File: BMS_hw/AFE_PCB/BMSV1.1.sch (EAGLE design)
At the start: 293 parts, among them IC1 MC33771BEP, IC10 TLP152-COUPLERTOSHIBA, IC11 TLP152-COUPLERTOSHIBA, IC2 SFH6156-1, IC3 MIC28515V1, IC7 SFH6156-1, IC8 SFH6156-1, IC9 TLP152-COUPLERTOSHIBA, Q1 IRLML5203, Q2 SI2392ADS-T1-GE3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

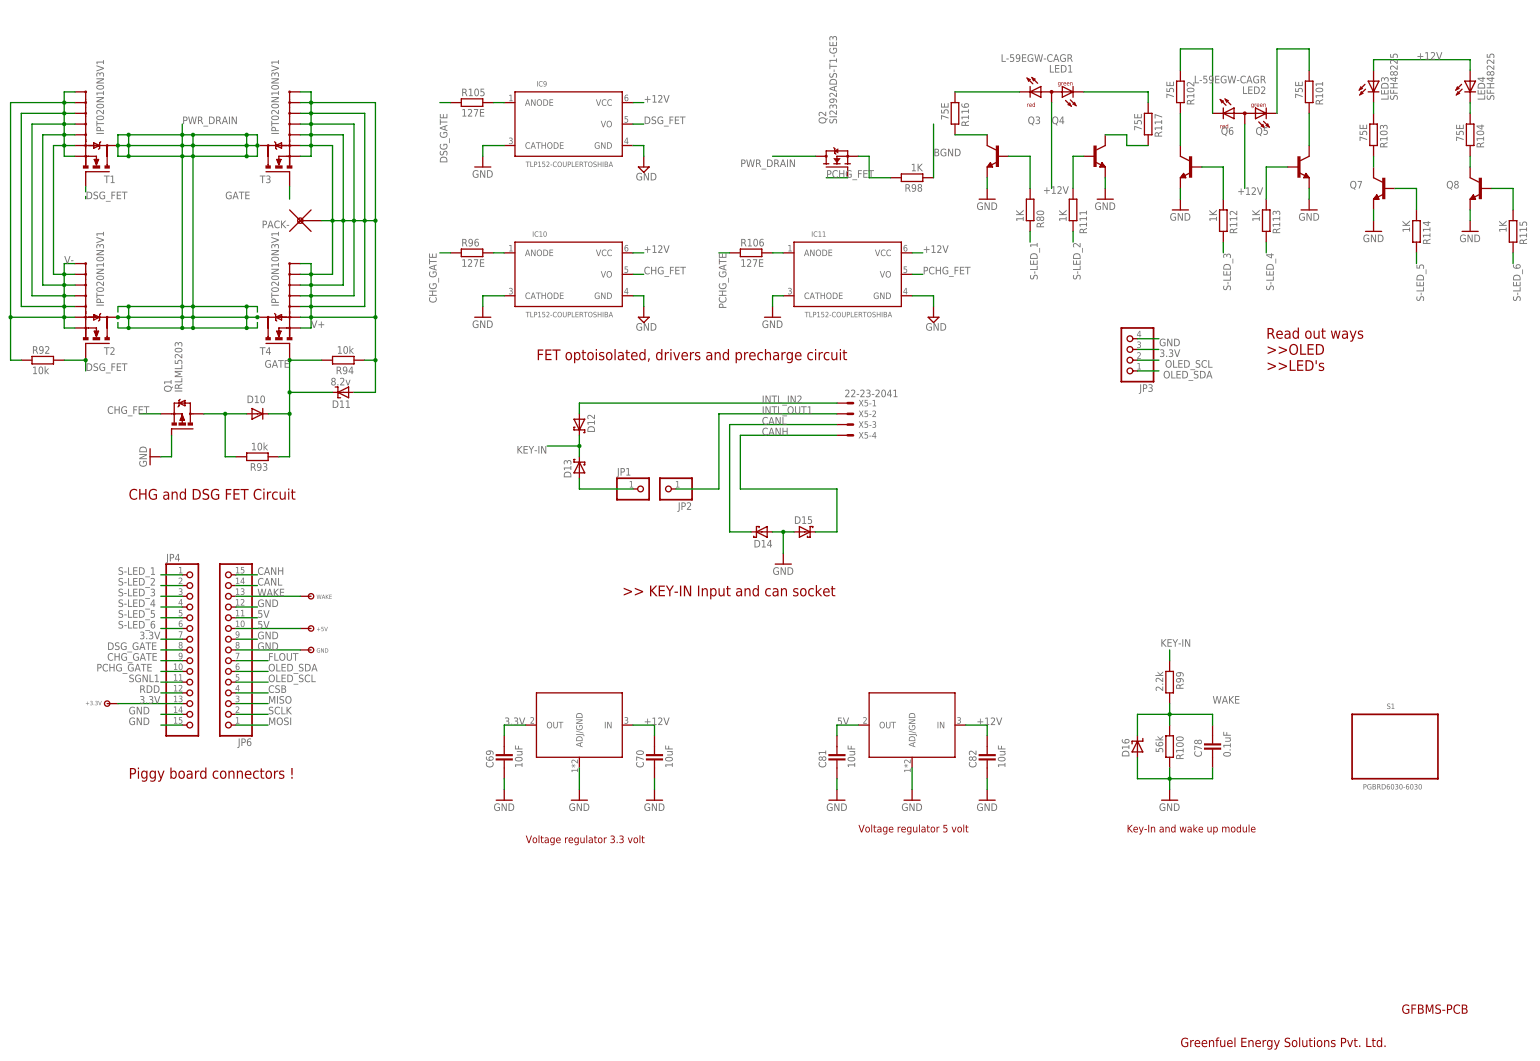
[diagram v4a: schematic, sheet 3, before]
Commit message: updated afe shmetatic rectification stage of MCU PCB
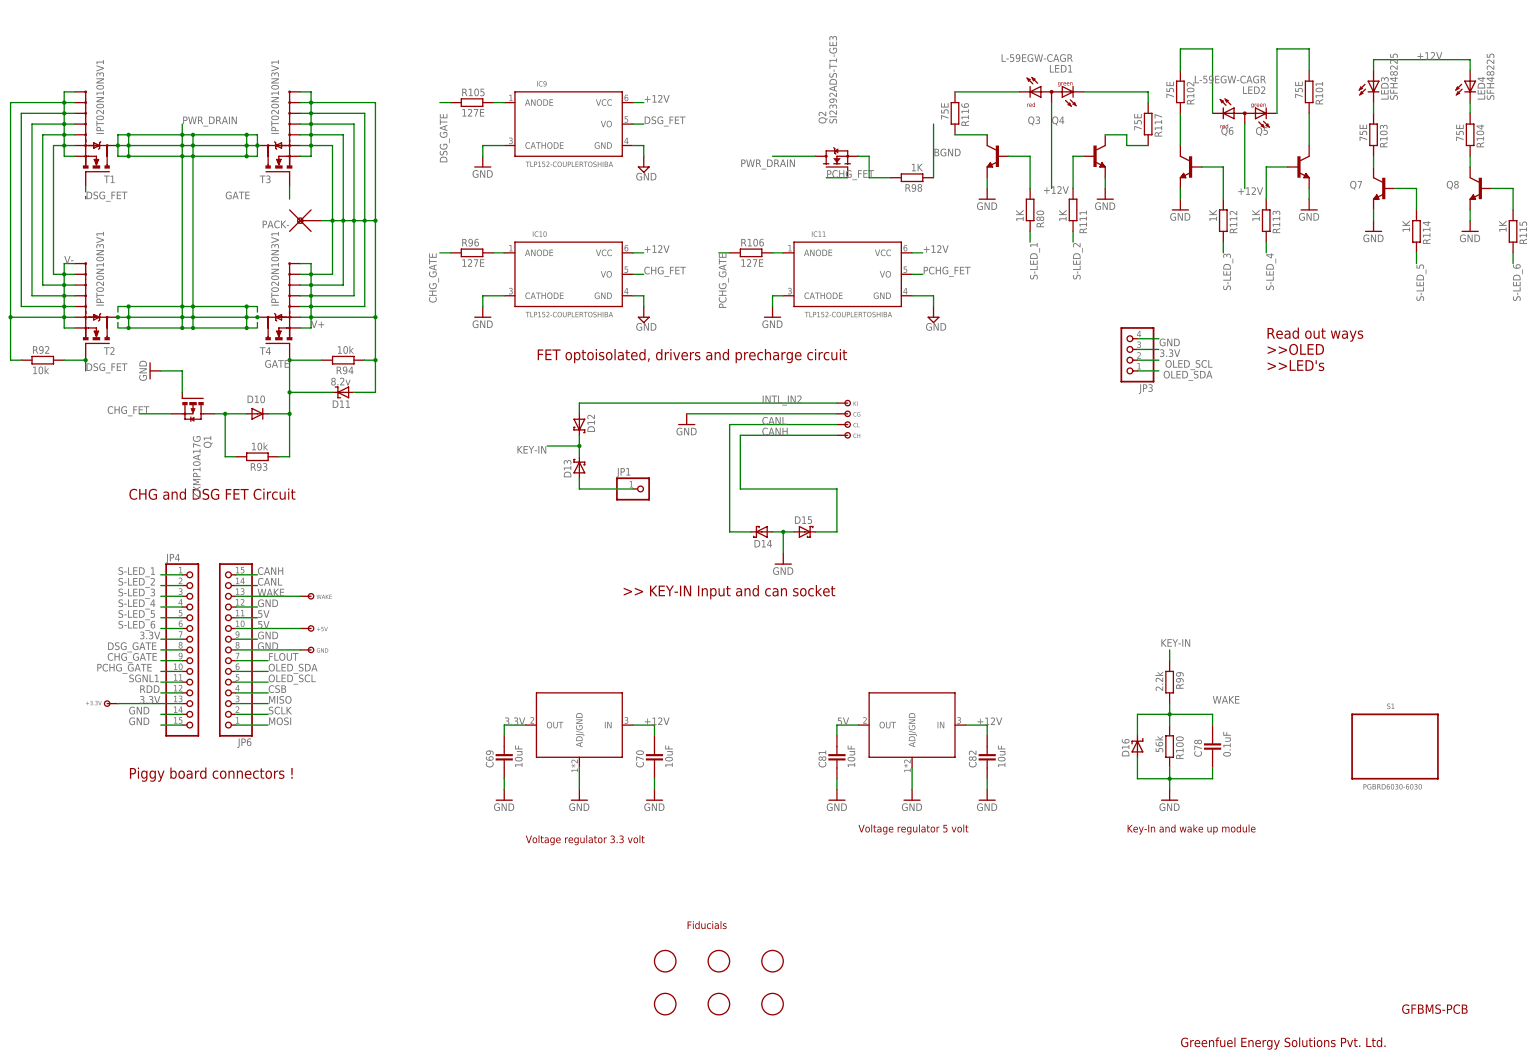
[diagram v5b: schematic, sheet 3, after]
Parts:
- removed +12V: TP-SMD60, simpa:TP-SMD60
- removed JP2: (no value), adafruit:PINHD-1X1CB
- removed X5: 22-23-2041, GreenFuel:22-23-2041
- added CG, CH, CL, KI: TPTH7035, simpa:TPTH7035
- added FD1, FD2, FD3, FD4, FD5, FD6: FIDUCIAL, adafruit:FIDUCIAL
- C90, C91: device ipc-7351-capacitor:POLARISED_CASE_B -> ipc-7351-capacitor:POLARISED_CASE_F
- Q1: value IRLML5203 -> ZXMP10A17G; device transistor-power:IRLML5203 -> GreenFuel:ZXMP10A17G
- R108: device ipc-7351-resistor:RESISTOR_0603 -> ipc-7351-resistor:RESISTOR_0402
- R119, R31, R95, R97: device ipc-7351-resistor:RESISTOR_0402 -> ipc-7351-resistor:RESISTOR_0603
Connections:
- removed net INTL_OUT1: JP2.1, X5-2.S
- net +12V: no longer +12V.P$1
- net CANH: now also CH.P$1; no longer X5-4.S
- net CANL: now also CL.P$1; no longer X5-3.S
- net CB_14+/14_C: no longer C63.2, C64.2, C90.+, IC3.VIN, IC3.VIN@1, IC3.VIN@2, IC3.VIN@3, IC3.VIN@4, IC3.VIN@5, IC3.VIN@6, R79.1
- net CELL14+: now also C63.2, C64.2, C90.+, IC3.VIN, IC3.VIN@1, IC3.VIN@2, IC3.VIN@3, IC3.VIN@4, IC3.VIN@5, IC3.VIN@6, R79.1
- net GND: now also CG.P$1
- net INTL_IN2: now also KI.P$1; no longer X5-1.S
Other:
- note added: "Fiducials"

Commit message: updated
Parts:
- added R120: 10k, ipc-7351-resistor:RESISTOR_0603
- added R121: 5.23k, ipc-7351-resistor:RESISTOR_0603
- added R122, R123, R124: 0E, ipc-7351-resistor:RESISTOR_0402
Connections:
- new net N$62: JP6.3, R120.1, R121.1
- net BGND: now also R122.1, R123.1, R124.1
- net GND: now also R120.2, R122.2, R123.2, R124.2
- net MISO: now also R121.2; no longer JP6.3
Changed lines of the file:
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@@
 <?xml version="1.0" encoding="utf-8"?>
 <!DOCTYPE eagle SYSTEM "eagle.dtd">
-<eagle version="9.2.1">
+<eagle version="9.2.2">
 <drawing>
 <settings>
@@
 <layer number="91" name="Nets" color="2" fill="1" visible="yes" active="yes"/>
 <layer number="92" name="Busses" color="1" fill="1" visible="yes" active="yes"/>
-<layer number="93" name="Pins" color="2" fill="1" visible="no" active="yes"/>
+<layer number="93" name="Pins" color="2" fill="1" visible="yes" active="yes"/>
 <layer number="94" name="Symbols" color="4" fill="1" visible="yes" active="yes"/>
 <layer number="95" name="Names" color="7" fill="1" visible="yes" active="yes"/>
@@
 <part name="FD5" library="adafruit" deviceset="FIDUCIAL" device=""/>
 <part name="FD6" library="adafruit" deviceset="FIDUCIAL" device=""/>
+<part name="R120" library="ipc-7351-resistor" deviceset="RESISTOR_" device="0603" value="10k"/>
+<part name="R121" library="ipc-7351-resistor" deviceset="RESISTOR_" device="0603" value="5.23k"/>
+<part name="GND78" library="supply1" library_urn="urn:adsk.eagle:library:371" deviceset="GND" device=""/>
+<part name="R122" library="ipc-7351-resistor" deviceset="RESISTOR_" device="0402" value="0E"/>
+<part name="R123" library="ipc-7351-resistor" deviceset="RESISTOR_" device="0402" value="0E"/>
+<part name="R124" library="ipc-7351-resistor" deviceset="RESISTOR_" device="0402" value="0E"/>
 </parts>
 <sheets>
@@
 <attribute name="NAME" x="326.39" y="70.485" size="1.016" layer="95" font="vector" ratio="12"/>
 </instance>
+<instance part="R122" gate="G$1" x="137.16" y="30.48" smashed="yes">
+<attribute name="NAME" x="134.62" y="32.004" size="1.778" layer="95" font="vector" ratio="12"/>
+<attribute name="VALUE" x="134.62" y="27.178" size="1.778" layer="96" font="vector" ratio="12"/>
+</instance>
+<instance part="R123" gate="G$1" x="137.16" y="22.86" smashed="yes">
+<attribute name="NAME" x="134.62" y="24.384" size="1.778" layer="95" font="vector" ratio="12"/>
+<attribute name="VALUE" x="134.62" y="19.558" size="1.778" layer="96" font="vector" ratio="12"/>
+</instance>
+<instance part="R124" gate="G$1" x="137.16" y="15.24" smashed="yes">
+<attribute name="NAME" x="134.62" y="16.764" size="1.778" layer="95" font="vector" ratio="12"/>
+<attribute name="VALUE" x="134.62" y="11.938" size="1.778" layer="96" font="vector" ratio="12"/>
+</instance>
 </instances>
 <busses>
@@
 <wire x1="236.22" y1="132.08" x2="236.22" y2="134.62" width="0.1524" layer="91"/>
 </segment>
+<segment>
+<pinref part="R122" gate="G$1" pin="2"/>
+<wire x1="142.24" y1="30.48" x2="149.86" y2="30.48" width="0.1524" layer="91"/>
+<wire x1="149.86" y1="30.48" x2="149.86" y2="22.86" width="0.1524" layer="91"/>
+<pinref part="R123" gate="G$1" pin="2"/>
+<wire x1="149.86" y1="22.86" x2="142.24" y2="22.86" width="0.1524" layer="91"/>
+<pinref part="R124" gate="G$1" pin="2"/>
+<wire x1="142.24" y1="15.24" x2="149.86" y2="15.24" width="0.1524" layer="91"/>
+<wire x1="149.86" y1="15.24" x2="149.86" y2="22.86" width="0.1524" layer="91"/>
+<junction x="149.86" y="22.86"/>
+<label x="149.86" y="22.86" size="1.778" layer="95"/>
+</segment>
 </net>
 <net name="CB_8/7_C" class="0">
@@
 <label x="25.4" y="43.18" size="1.778" layer="95"/>
 </segment>
+<segment>
+<pinref part="R122" gate="G$1" pin="1"/>
+<wire x1="132.08" y1="30.48" x2="124.46" y2="30.48" width="0.1524" layer="91"/>
+<wire x1="124.46" y1="30.48" x2="124.46" y2="22.86" width="0.1524" layer="91"/>
+<pinref part="R123" gate="G$1" pin="1"/>
+<wire x1="124.46" y1="22.86" x2="132.08" y2="22.86" width="0.1524" layer="91"/>
+<pinref part="R124" gate="G$1" pin="1"/>
+<wire x1="132.08" y1="15.24" x2="124.46" y2="15.24" width="0.1524" layer="91"/>
+<wire x1="124.46" y1="15.24" x2="124.46" y2="22.86" width="0.1524" layer="91"/>
+<junction x="124.46" y="22.86"/>
+<label x="116.84" y="22.86" size="1.778" layer="95"/>
+</segment>
 </net>
 <net name="N$68" class="0">
@@
 <instance part="FD5" gate="G$1" x="182.88" y="22.86" smashed="yes"/>
 <instance part="FD6" gate="G$1" x="170.18" y="22.86" smashed="yes"/>
+<instance part="R120" gate="G$1" x="99.06" y="86.36" smashed="yes" rot="R270">
+<attribute name="NAME" x="100.584" y="88.9" size="1.778" layer="95" rot="R270"/>
+<attribute name="VALUE" x="95.758" y="88.9" size="1.778" layer="96" rot="R270"/>
+</instance>
+<instance part="R121" gate="G$1" x="109.22" y="93.98" smashed="yes">
+<attribute name="NAME" x="106.68" y="95.504" size="1.778" layer="95"/>
+<attribute name="VALUE" x="106.68" y="90.678" size="1.778" layer="96"/>
+</instance>
+<instance part="GND78" gate="1" x="99.06" y="73.66" smashed="yes">
+<attribute name="VALUE" x="96.52" y="71.12" size="1.778" layer="96"/>
+</instance>
 </instances>
 <busses>
@@
 <pinref part="CG" gate="G$1" pin="P$1"/>
 </segment>
+<segment>
+<pinref part="R120" gate="G$1" pin="2"/>
+<pinref part="GND78" gate="1" pin="GND"/>
+<wire x1="99.06" y1="81.28" x2="99.06" y2="76.2" width="0.1524" layer="91"/>
+</segment>
 </net>
 <net name="CHG_FET" class="0">
@@
 </segment>
 </net>
-<net name="MISO" class="0">
-<segment>
-<pinref part="JP6" gate="A" pin="3"/>
-<wire x1="68.58" y1="93.98" x2="76.2" y2="93.98" width="0.1524" layer="91"/>
-<label x="76.2" y="93.98" size="1.778" layer="95" font="vector" ratio="12"/>
-</segment>
-</net>
 <net name="SCLK" class="0">
 <segment>
@@
 </segment>
 </net>
+<net name="N$62" class="0">
+<segment>
+<pinref part="R121" gate="G$1" pin="1"/>
+<pinref part="R120" gate="G$1" pin="1"/>
+<wire x1="104.14" y1="93.98" x2="99.06" y2="93.98" width="0.1524" layer="91"/>
+<wire x1="99.06" y1="93.98" x2="99.06" y2="91.44" width="0.1524" layer="91"/>
+<pinref part="JP6" gate="A" pin="3"/>
+<wire x1="68.58" y1="93.98" x2="99.06" y2="93.98" width="0.1524" layer="91"/>
+<junction x="99.06" y="93.98"/>
+</segment>
+</net>
+<net name="MISO" class="0">
+<segment>
+<pinref part="R121" gate="G$1" pin="2"/>
+<wire x1="114.3" y1="93.98" x2="119.38" y2="93.98" width="0.1524" layer="91"/>
+<label x="116.84" y="93.98" size="1.778" layer="95"/>
+</segment>
+</net>
